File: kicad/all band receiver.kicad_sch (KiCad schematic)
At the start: 33 parts, among them J1 AudioJack3_SwitchT, J2 Conn_01x01_Socket, J3 Conn_01x02_Socket, Q1 2N4401, U1 LM386

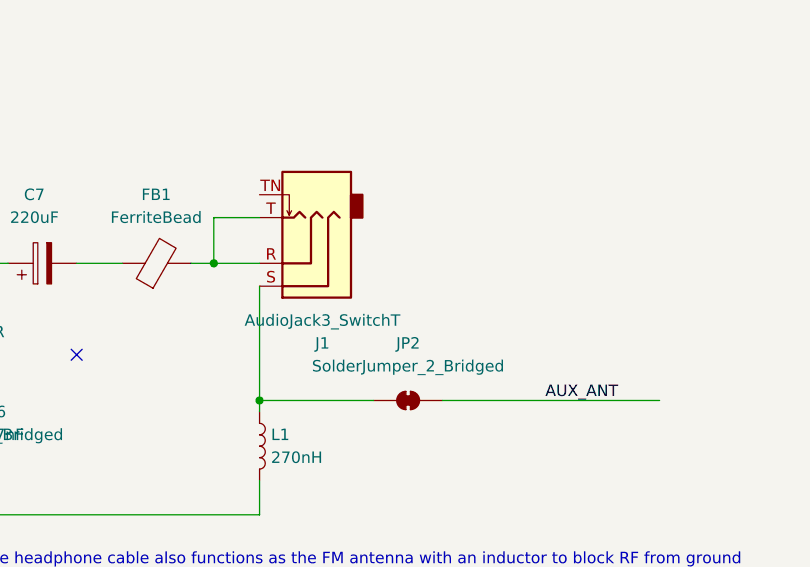
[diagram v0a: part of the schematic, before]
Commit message: moved (almost) all smt components to bottom side so manufacturing is cheaper. chanded audio connector on upper side to thruhole for easy soldering
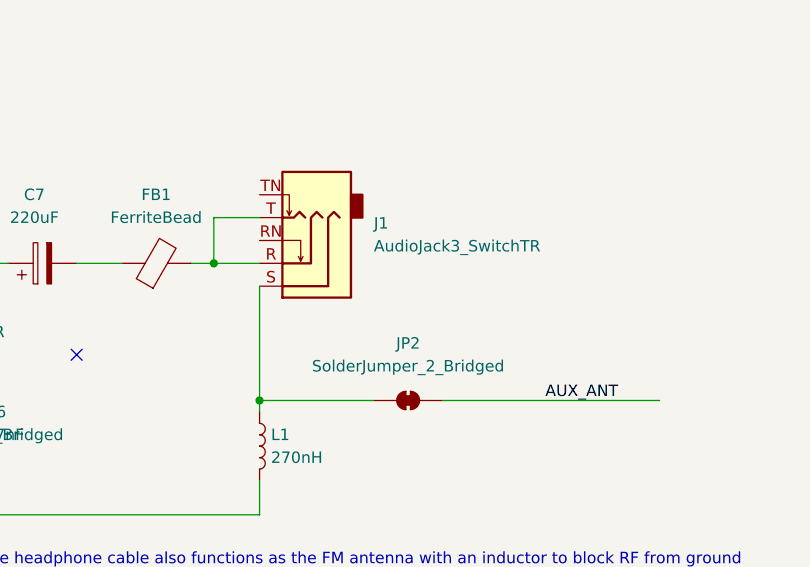
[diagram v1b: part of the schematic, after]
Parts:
- removed J1: AudioJack3_SwitchT, Connector_Audio:Jack_3.5mm_CUI_SJ-3524-SMT_Horizontal, symbol Connector_Audio:AudioJack3_SwitchT
- added J1: AudioJack3_SwitchTR, Connector_Audio:Jack_3.5mm_CUI_SJ1-3525N_Horizontal, symbol Connector_Audio:AudioJack3_SwitchTR
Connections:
- net at JP2.2 (B), L1.1: now also J1.S
- net at FB1.2: now also J1.R, J1.T
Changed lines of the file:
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@@
 		)
 		(instances
-			(project ""
+			(project "all band receiver"
 				(path "/cfb87c2d-93e9-4044-8e22-776b72077ce5"
 					(reference "BT1")
@@
 		)
 		(instances
-			(project ""
+			(project "all band receiver"
 				(path "/cfb87c2d-93e9-4044-8e22-776b72077ce5"
 					(reference "JP1")
@@
 	)
 	(symbol
-		(lib_id "Connector_Audio:AudioJack3_SwitchT")
+		(lib_id "Connector_Audio:AudioJack3_SwitchTR")
 		(at 207.01 86.36 180)
 		(unit 1)
@@
 		(on_board yes)
 		(dnp no)
+		(fields_autoplaced yes)
 		(property "Reference" "J1"
-			(at 208.915 95.25 0)
-			(effects
-				(font
-					(size 1.27 1.27)
-				)
-			)
-		)
-		(property "Value" "AudioJack3_SwitchT"
-			(at 208.915 92.71 0)
-			(effects
-				(font
-					(size 1.27 1.27)
-				)
-			)
-		)
-		(property "Footprint" "Connector_Audio:Jack_3.5mm_CUI_SJ-3524-SMT_Horizontal"
+			(at 214.63 81.9149 0)
+			(effects
+				(font
+					(size 1.27 1.27)
+				)
+				(justify right)
+			)
+		)
+		(property "Value" "AudioJack3_SwitchTR"
+			(at 214.63 84.4549 0)
+			(effects
+				(font
+					(size 1.27 1.27)
+				)
+				(justify right)
+			)
+		)
+		(property "Footprint" "Connector_Audio:Jack_3.5mm_CUI_SJ1-3525N_Horizontal"
 			(at 207.01 86.36 0)
 			(effects
@@
 			)
 		)
-		(property "Description" "Audio Jack, 3 Poles (Stereo / TRS), Switched T Pole (Normalling)"
+		(property "Description" "Audio Jack, 3 Poles (Stereo / TRS), Switched TR Poles (Normalling)"
 			(at 207.01 86.36 0)
 			(effects
@@
 			)
 		)
+		(pin "T"
+		)
+		(pin "TN"
+		)
 		(pin "R"
 		)
+		(pin "RN"
+		)
 		(pin "S"
 		)
-		(pin "TN"
-		)
-		(pin "T"
-		)
-		(instances
+		(instances

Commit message: production
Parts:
- BT1: Mouser Price/Stock https://www.mouser.co.uk/ProductDetail/Keystone-Electronics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 -> (none)
- C1: DigiKey Part Number (none) -> 399-C0805C101J5GACTUCT-ND; LCSC (none) -> C1790; Mouser Part Number (none) -> 80-C0805C101K1HACTU
- C2, C3: DigiKey Part Number (none) -> 399-C0805C102K5RACTUCT-ND; LCSC (none) -> C46653; Mouser Part Number (none) -> 187-CL21B102KBANNND
- C4: DigiKey Part Number (none) -> 311-1140-1-ND; LCSC (none) -> C28233; Mouser Part Number (none) -> 187-CL21B104MACNNNC
- C5: DigiKey Part Number (none) -> 311-1133-1-ND; LCSC (none) -> C1744; Mouser Part Number (none) -> 791-0805N472J500CT
- C6: DigiKey Part Number (none) -> 399-C0805C473K5RACTUCT-ND; LCSC (none) -> C53134; Mouser Part Number (none) -> 791-0805B473J500CT
- C7: DigiKey Part Number (none) -> 478-APA0608221M010RCT-ND; LCSC (none) -> C3345; Mouser Part Number (none) -> 140-VZL221M1CTR-0607
- C8: DigiKey Part Number (none) -> 732-6401-1-ND; LCSC (none) -> C263972; Mouser Part Number (none) -> 710-865060640001
- C9: DigiKey Part Number (none) -> 587-1300-1-ND; LCSC (none) -> C15850; Mouser Part Number (none) -> 187-CL21A106KQFNFNE
- D1: DigiKey Part Number (none) -> 497-5558-1-ND; LCSC (none) -> C222251; Mouser Part Number (none) -> 511-BAT41ZFILM
- FB1: DigiKey Part Number (none) -> MH2029-070YCT-ND; LCSC (none) -> C1017; Mouser Part Number (none) -> 70-ILBB0805ER110V
- J1: value AudioJack3_SwitchTR -> CUI_SJ1-3525N; DigiKey Part Number (none) -> SJ1-3525NG; Mouser Part Number (none) -> 490-SJ1-3525NG-GR
- J2: footprint Connector_Wire:SolderWire-0.5sqmm_1x01_D0.9mm_OD2.1mm -> Connector_PinHeader_2.54mm:PinHeader_1x01_P2.54mm_Horizontal; now left out of the parts list
- J3: now fitted; now left out of the parts list
- L1: DigiKey Part Number (none) -> 118-CE201210-R27JCT-ND; LCSC (none) -> C108271; Mouser Part Number (none) -> 70-IMC0805ERR27J01
- Q1: DigiKey Part Number (none) -> 4786-MMBT4401CT-ND; LCSC (none) -> C31776; Mouser Part Number (none) -> 637-MMBT4401
- R1: value ~ -> P091S-QC15BR; DigiKey Part Number (none) -> 987-1284-ND; LCSC (none) -> C17464898; Mouser Part Number (none) -> 858-P091SFC20BR10K
- R2, R7: DigiKey Part Number (none) -> P10KACT-ND; LCSC (none) -> C17414; Mouser Part Number (none) -> 71-CRCW0805-10K-E3
- R3, R4: DigiKey Part Number (none) -> P10MACT-ND; LCSC (none) -> C114525; Mouser Part Number (none) -> 603-RC0805FR-0710ML
- R5: DigiKey Part Number (none) -> P100ACT-ND; LCSC (none) -> C17408; Mouser Part Number (none) -> 603-AC0805FR-7W100RL
- R6: DigiKey Part Number (none) -> P100KACT-ND; LCSC (none) -> C149504; Mouser Part Number (none) -> 652-CR0805FX-1003ELF
- R8: DigiKey Part Number (none) -> RMCF0805JT10R0CT-ND; LCSC (none) -> C17415; Mouser Part Number (none) -> 603-AC0805JR-0710RL
- R9: DigiKey Part Number (none) -> A126346CT-ND; LCSC (none) -> C17379; Mouser Part Number (none) -> 652-CR0805FX-1201ELF
- TP1, TP2, TP3, TP4: now left out of the parts list
- U1: DigiKey Part Number (none) -> LM386MX-1/NOPBCT-ND; LCSC (none) -> C23573; Mouser Part Number (none) -> 926-LM386MX-1/NOPB
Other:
- moved on the sheet: C4
